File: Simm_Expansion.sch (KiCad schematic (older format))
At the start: 16 parts, among them J10 Mem_on_off, U40 GAL20V8_DIP, U41 74LS157, U42 74LS175, U43 DRAM_1MB_4bit, U44 DRAM_1MB_4bit

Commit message: SMD ram
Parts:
- R110, R111: footprint Atari:R_Axial_DIN0207_L3.6mm_D2.2mm_P10.16mm_Horizontal -> Resistor_SMD:R_1206_3216Metric_Pad1.42x1.75mm_HandSolder
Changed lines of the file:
@@
 F 0 "R110" V 1175 4350 50  0000 C CNN
 F 1 "33" V 1075 4350 50  0000 C CNN
-F 2 "Atari:R_Axial_DIN0207_L3.6mm_D2.2mm_P10.16mm_Horizontal" V 1105 4350 50  0001 C CNN
+F 2 "Resistor_SMD:R_1206_3216Metric_Pad1.42x1.75mm_HandSolder" V 1105 4350 50  0001 C CNN
 F 3 "~" H 1175 4350 50  0001 C CNN
 	1    1175 4350
@@
 F 0 "R111" V 6025 2875 50  0000 C CNN
 F 1 "33" V 5925 2875 50  0000 C CNN
-F 2 "Atari:R_Axial_DIN0207_L3.6mm_D2.2mm_P10.16mm_Horizontal" V 5955 2875 50  0001 C CNN
+F 2 "Resistor_SMD:R_1206_3216Metric_Pad1.42x1.75mm_HandSolder" V 5955 2875 50  0001 C CNN
 F 3 "~" H 6025 2875 50  0001 C CNN
 	1    6025 2875

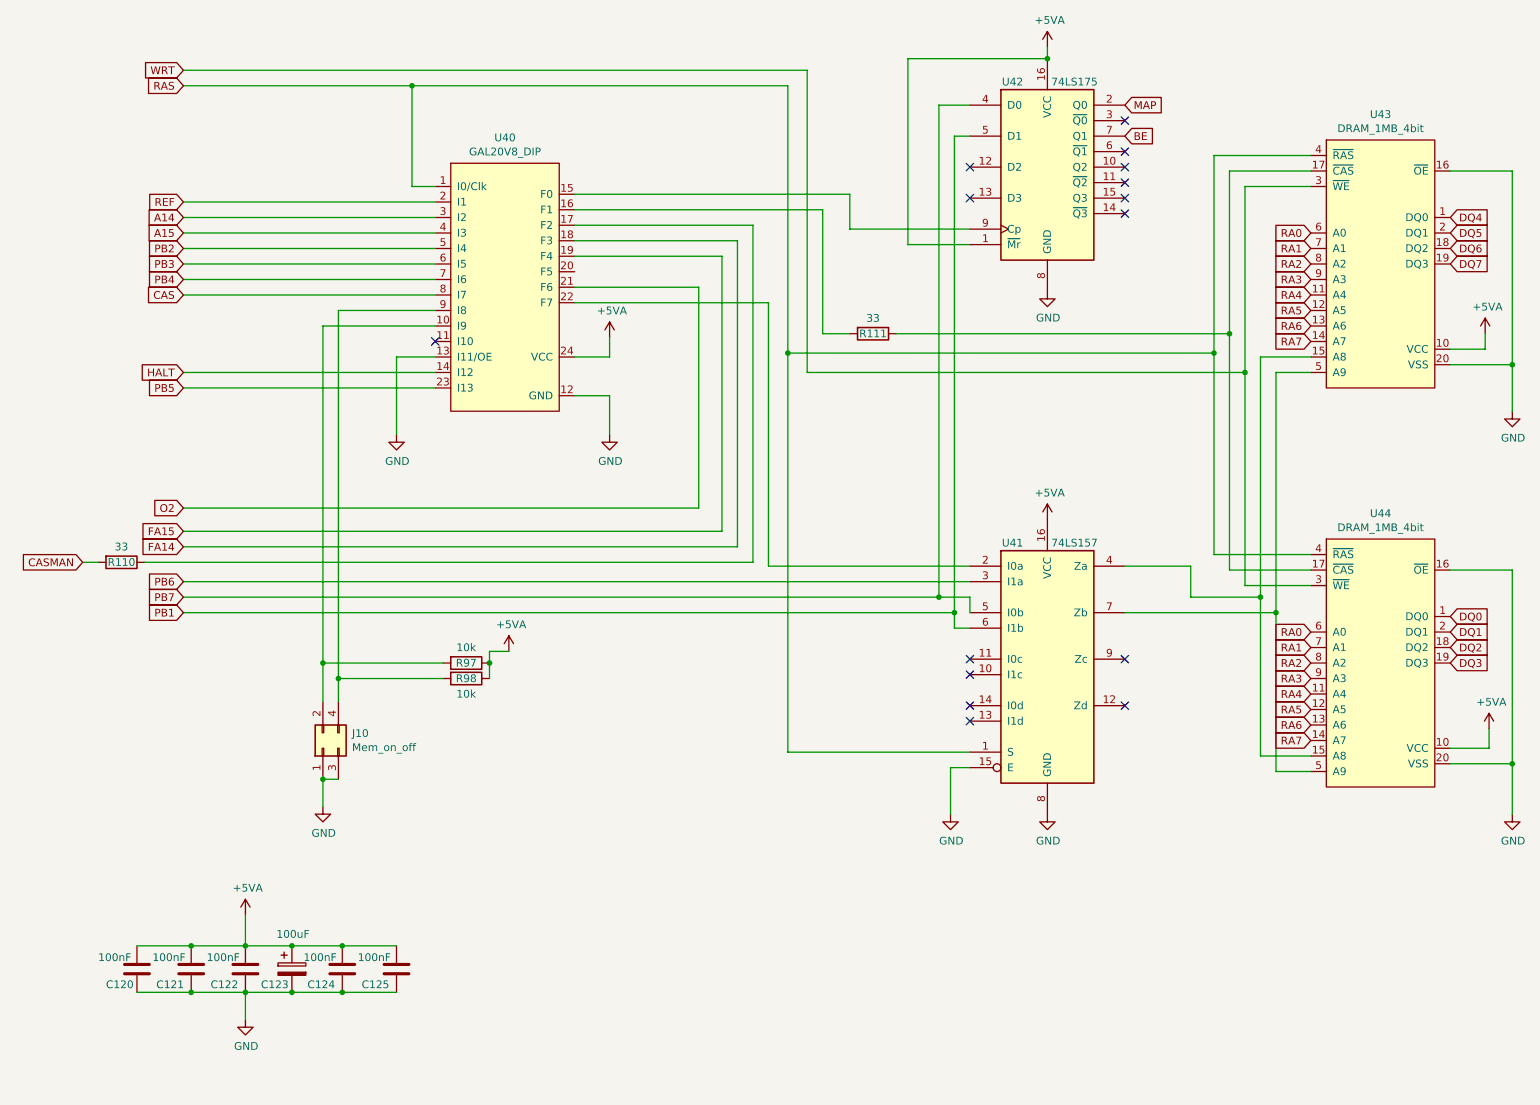
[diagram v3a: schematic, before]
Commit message: add 74ls04
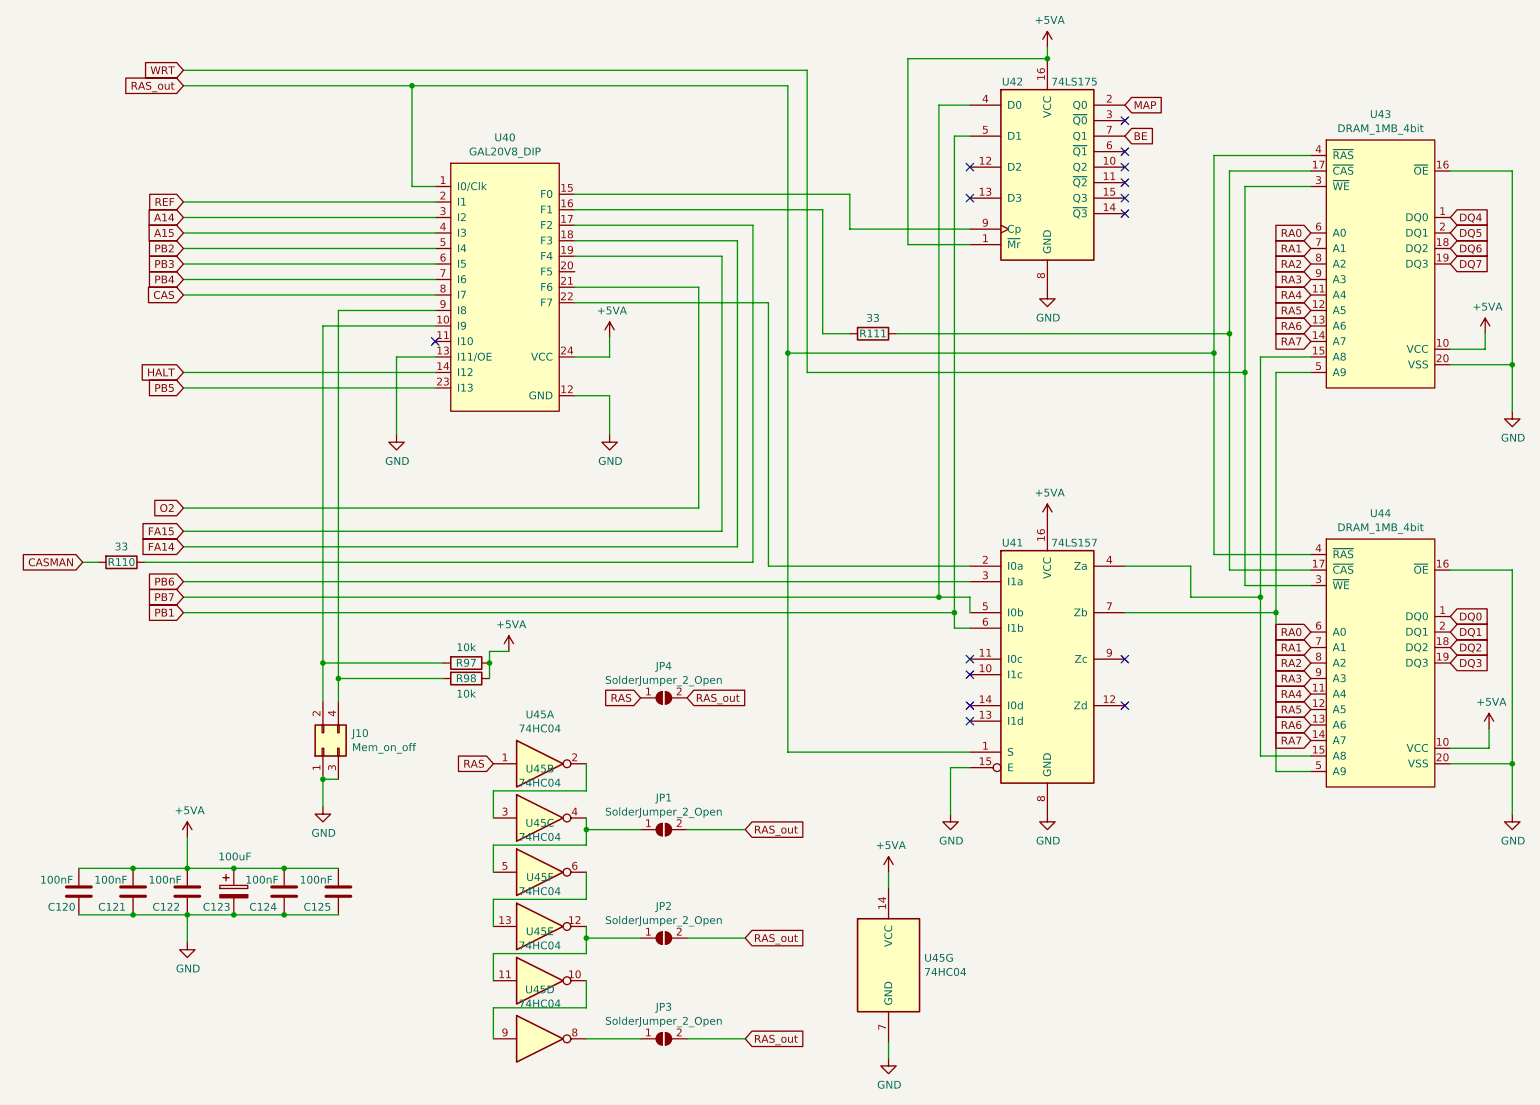
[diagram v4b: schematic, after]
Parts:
- added JP1, JP2, JP3, JP4: SolderJumper_2_Open, Jumper:SolderJumper-2_P1.3mm_Open_RoundedPad1.0x1.5mm, symbol Jumper:SolderJumper_2_Open
- added U45: 74HC04, Package_SO:SOIC-14_3.9x8.7mm_P1.27mm, symbol 74xx:74HC04
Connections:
- net +5VA: now also U45.14 (VCC)
- net GND: now also U45.7 (GND)
- net RAS: now also JP4.1 (A), U45.1; no longer U40.1 (I0/Clk), U41.1 (S), U43.4 (~RAS), U44.4 (~RAS)
- new net: U45.2, U45.3
- new net: JP1.1 (A), U45.4, U45.5
- new net: U45.13, U45.6
- new net: JP3.1 (A), U45.8
- new net: U45.10, U45.9
- new net: JP2.1 (A), U45.11, U45.12
- new net RAS_out: JP1.2 (B), JP2.2 (B), JP3.2 (B), JP4.2 (B), U40.1 (I0/Clk), U41.1 (S), U43.4 (~RAS), U44.4 (~RAS)
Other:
- moved on the sheet: C120, C121, C122, C123, C124, C125

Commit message: Gerber
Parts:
- removed JP1, JP2, JP3, JP4: SolderJumper_2_Open, Jumper:SolderJumper-2_P1.3mm_Open_RoundedPad1.0x1.5mm, symbol Jumper:SolderJumper_2_Open
- added J12: Conn_02x04_Odd_Even, Connector_PinHeader_2.00mm:PinHeader_2x04_P2.00mm_Vertical, symbol Connector_Generic:Conn_02x04_Odd_Even
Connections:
- net RAS: now also J12.2 (Pin_2)
- net RAS_out: now also J12.1 (Pin_1), J12.3 (Pin_3), J12.5 (Pin_5), J12.7 (Pin_7)
- net at U45.4, U45.5: now also J12.8 (Pin_8)
- net at U45.8: now also J12.4 (Pin_4)
- net at U45.11, U45.12: now also J12.6 (Pin_6)
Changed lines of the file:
@@
 	3575 6175 4175 6175
-Wire Wire Line
-	4175 6175 4175 6075
 Wire Wire Line
 	3575 6700 3575 6525
@@
 	3575 6875 4175 6875
 Wire Wire Line
-	4175 6875 4175 6775
-Wire Wire Line
 	3575 7425 3575 7225
 Wire Wire Line
@@
 Text GLabel 3575 5650 0    50   Input ~ 0
 RAS
+Text GLabel 5175 6650 2    50   Input ~ 0
+RAS_out
+Text GLabel 5175 6800 2    50   Input ~ 0
+RAS
 $Comp
-L Jumper:SolderJumper_2_Open JP1
-U 1 1 62D065C5
-P 4675 6075
-F 0 "JP1" H 4675 6280 50  0000 C CNN
-F 1 "SolderJumper_2_Open" H 4675 6189 50  0000 C CNN
-F 2 "Jumper:SolderJumper-2_P1.3mm_Open_RoundedPad1.0x1.5mm" H 4675 6075 50  0001 C CNN
-F 3 "~" H 4675 6075 50  0001 C CNN
-	1    4675 6075
-	1    0    0    -1
+L Connector_Generic:Conn_02x04_Odd_Even J12
+U 1 1 62D4E5EC
+P 4750 6550
+F 0 "J12" H 4800 6125 50  0000 C CNN
+F 1 "Conn_02x04_Odd_Even" H 4800 6216 50  0000 C CNN
+F 2 "Connector_PinHeader_2.00mm:PinHeader_2x04_P2.00mm_Vertical" H 4750 6550 50  0001 C CNN
+F 3 "~" H 4750 6550 50  0001 C CNN
+	1    4750 6550
+	-1   0    0    1
 $EndComp
 Wire Wire Line
-	4525 6075 4175 6075
-Connection ~ 4175 6075
+	4175 6700 4175 6875
 Wire Wire Line
-	4175 6075 4175 6000
-Text GLabel 5200 6075 2    50   Input ~ 0
-RAS_out
+	4175 6700 4300 6700
+Connection ~ 4175 6700
 Wire Wire Line
-	4825 6075 5200 6075
-$Comp
-L Jumper:SolderJumper_2_Open JP2
-U 1 1 62D17E6A
-P 4675 6775
-F 0 "JP2" H 4675 6980 50  0000 C CNN
-F 1 "SolderJumper_2_Open" H 4675 6889 50  0000 C CNN
-F 2 "Jumper:SolderJumper-2_P1.3mm_Open_RoundedPad1.0x1.5mm" H 4675 6775 50  0001 C CNN
-F 3 "~" H 4675 6775 50  0001 C CNN
-	1    4675 6775
-	1    0    0    -1
-$EndComp
-$Comp
-L Jumper:SolderJumper_2_Open JP3
-U 1 1 62D186E5
-P 4675 7425
-F 0 "JP3" H 4675 7630 50  0000 C CNN
-F 1 "SolderJumper_2_Open" H 4675 7539 50  0000 C CNN
-F 2 "Jumper:SolderJumper-2_P1.3mm_Open_RoundedPad1.0x1.5mm" H 4675 7425 50  0001 C CNN
-F 3 "~" H 4675 7425 50  0001 C CNN
-	1    4675 7425
-	1    0    0    -1
-$EndComp
+	4175 6175 4300 6175
+Connection ~ 4175 6175
 Wire Wire Line
-	4525 6775 4175 6775
-Connection ~ 4175 6775
+	4175 6000 4175 6175
 Wire Wire Line
-	4175 6775 4175 6700
-Text GLabel 5200 6775 2    50   Input ~ 0
-RAS_out
-Text GLabel 5200 7425 2    50   Input ~ 0
-RAS_out
+	4950 6650 5175 6650
 Wire Wire Line
-	5200 7425 4825 7425
+	4950 6550 4950 6650
+Connection ~ 4950 6650
 Wire Wire Line
-	4825 6775 5200 6775
-$Comp
-L Jumper:SolderJumper_2_Open JP4
-U 1 1 62D329BE
-P 4675 5225
-F 0 "JP4" H 4675 5430 50  0000 C CNN
-F 1 "SolderJumper_2_Open" H 4675 5339 50  0000 C CNN
-F 2 "Jumper:SolderJumper-2_P1.3mm_Open_RoundedPad1.0x1.5mm" H 4675 5225 50  0001 C CNN
-F 3 "~" H 4675 5225 50  0001 C CNN
-	1    4675 5225
-	1    0    0    -1
-$EndComp
-Text GLabel 4525 5225 0    50   Input ~ 0
-RAS
-Text GLabel 4825 5225 2    50   Input ~ 0
-RAS_out
+	4950 6350 4950 6450
 Wire Wire Line
-	4525 7425 4175 7425
+	4950 6450 4950 6550
+Connection ~ 4950 6450
+Connection ~ 4950 6550
+Wire Wire Line
+	4300 6450 4450 6450
+Wire Wire Line
+	4300 6450 4300 6700
+Wire Wire Line
+	4300 6175 4300 6350
+Wire Wire Line
+	4300 6350 4450 6350
+Wire Wire Line
+	4175 7425 4375 7425
+Wire Wire Line
+	4375 7425 4375 6550
+Wire Wire Line
+	4375 6550 4450 6550
+Wire Wire Line
+	5175 6800 4450 6800
+Wire Wire Line
+	4450 6800 4450 6650
 $EndSCHEMATC
